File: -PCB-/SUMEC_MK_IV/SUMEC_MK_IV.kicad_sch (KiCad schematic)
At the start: 0 parts

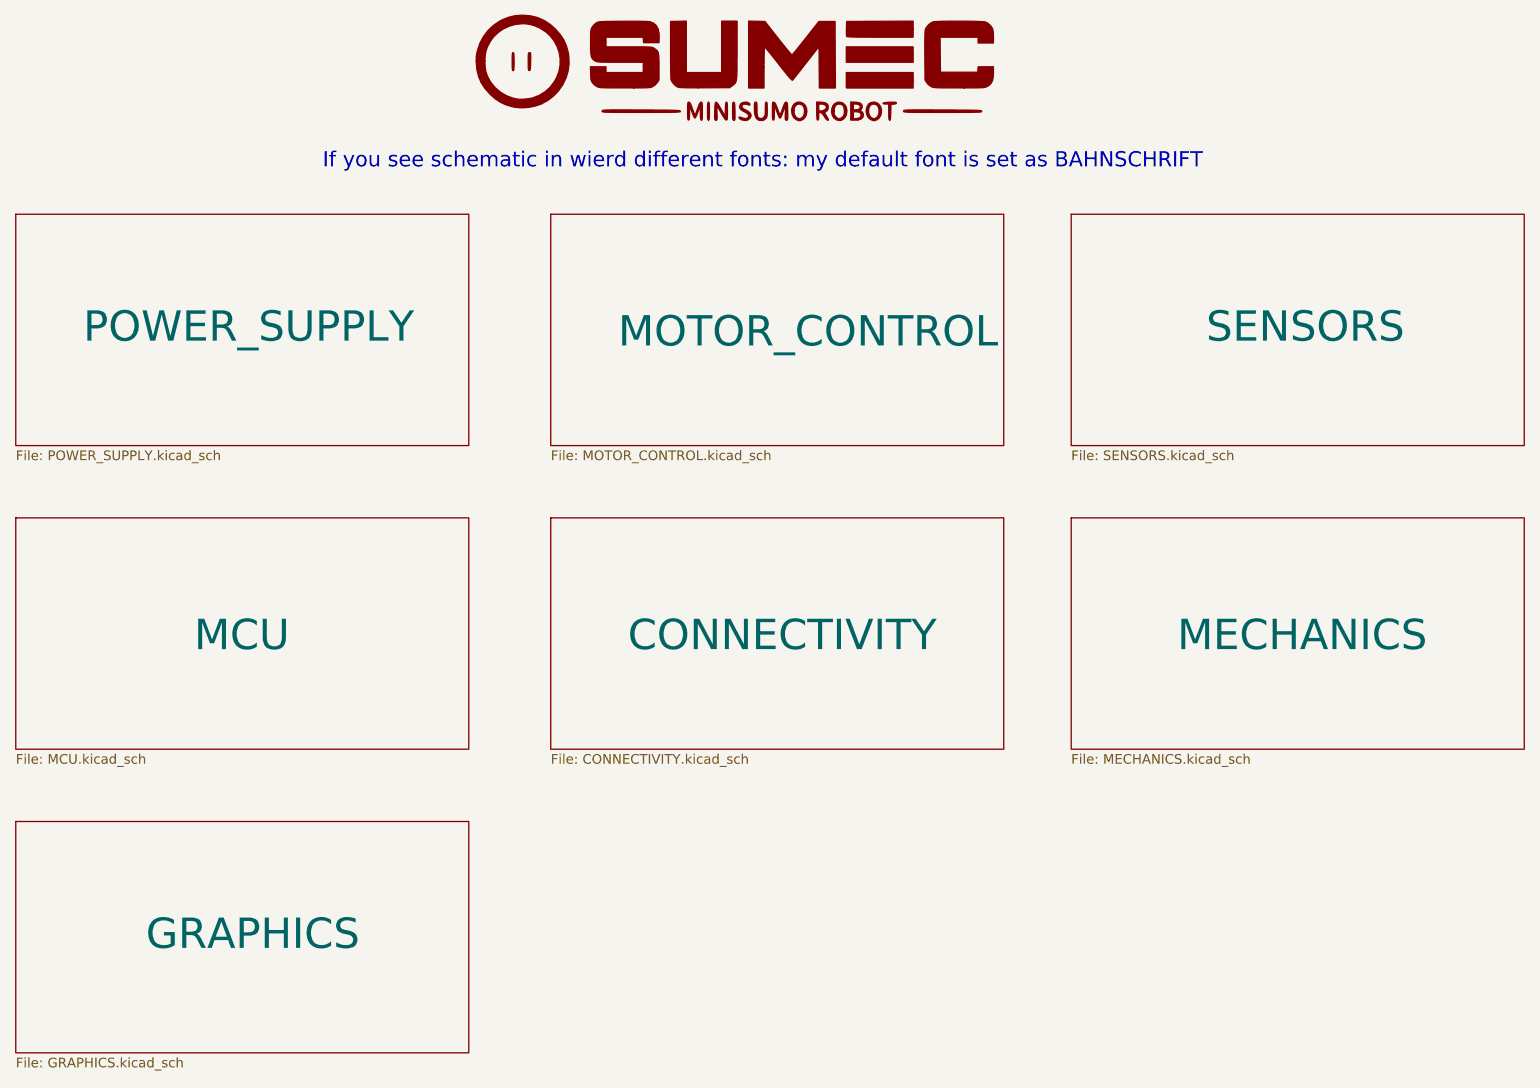
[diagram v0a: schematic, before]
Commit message: Minor text changes in schematic
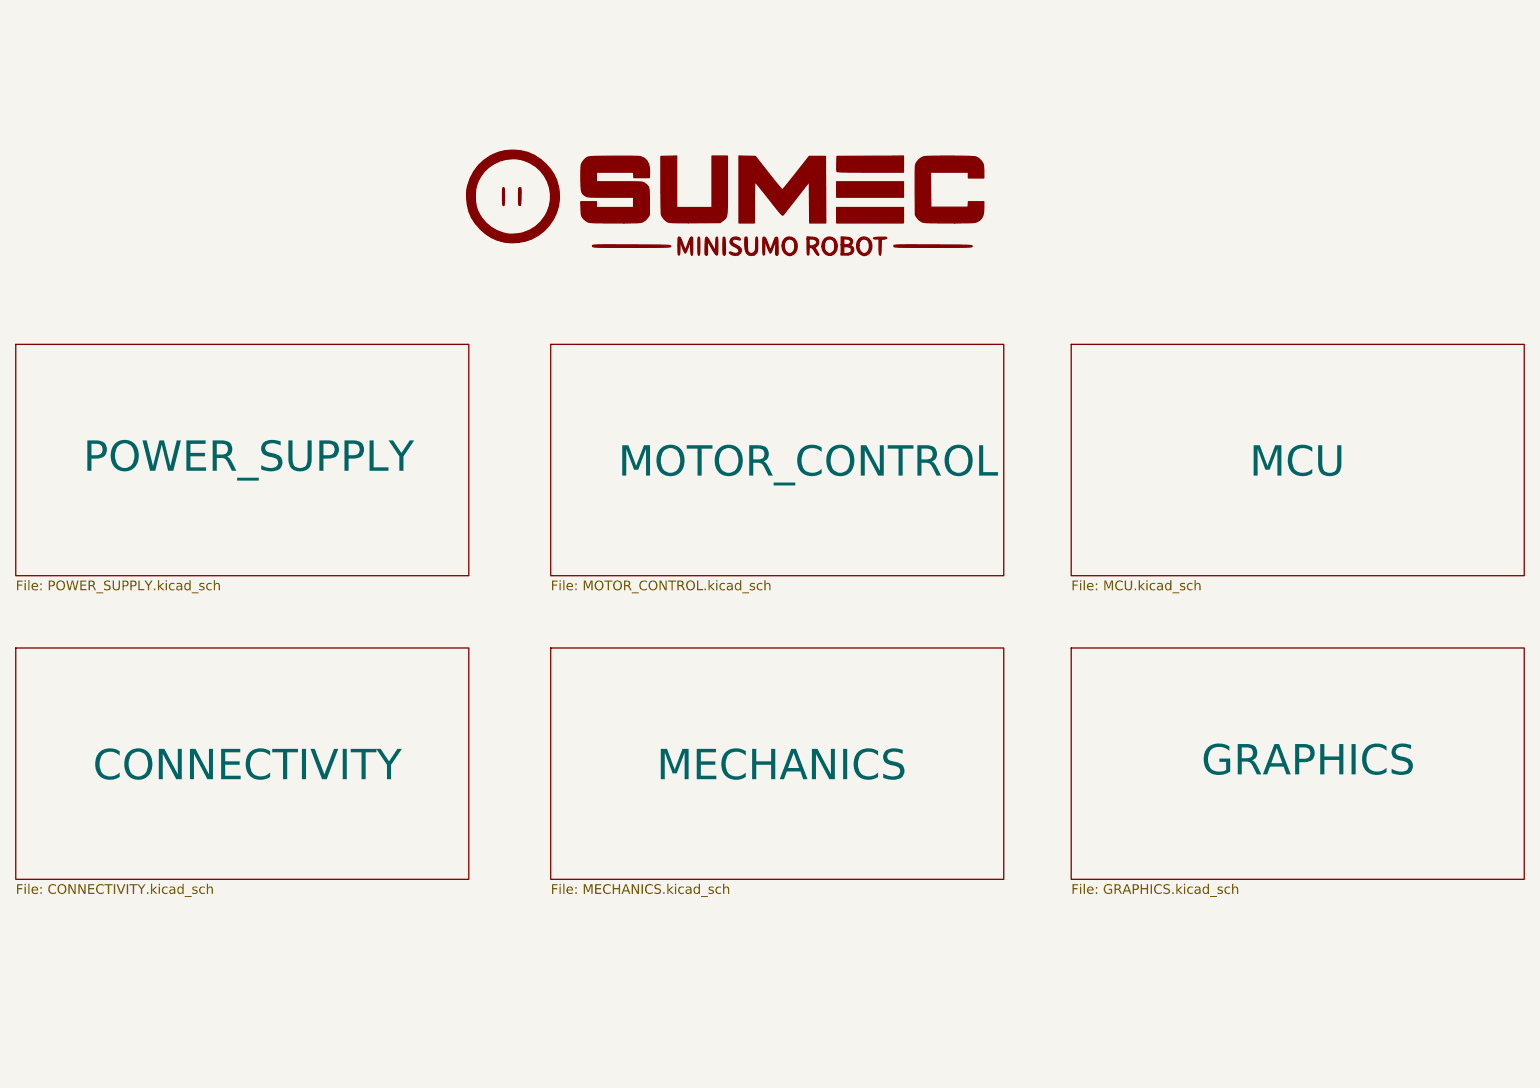
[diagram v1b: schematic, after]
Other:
- removed sheet SENSORS
- note removed: "If you see schematic in wierd different fonts: my default font is set as BAHNSCHRIFT"
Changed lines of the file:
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@@
 		(company "SPS NA PROSEKU")
 		(comment 1 "Made in Prague, Czech Republic")
-		(comment 2 "CONTACT: Savva Popov, menmenson09@gmail.com, +420 605 570 366")
-		(comment 3 "Made by Bismarx aka MenMenson")
+		(comment 2 "CONTACT: Savva Popov, savva.popov.sp@gmail.com, +420 605 570 366")
+		(comment 3 "Made by bismarx-v1")
 		(comment 4 "SUMEC MK IV aka SMD-V3 board")
-	)
-	(text "If you see schematic in wierd different fonts: my default font is set as BAHNSCHRIFT"
-		(exclude_from_sim no)
-		(at 147.32 41.91 0)
-		(effects
-			(font
-				(size 2 2)
-				(color 0 0 0 1)
-			)
-		)
 	)
 	(symbol
 		(lib_id "sumec_sch_lib:LOGO SMALL")
-		(at 142.24 30.48 0)
+		(at 140.97 48.26 0)
 		(unit 1)
 		(exclude_from_sim no)
@@
 		(fields_autoplaced yes)
 		(property "Reference" "#G1"
-			(at 142.24 19.8543 0)
+			(at 140.97 37.6343 0)
 			(effects
 				(font
@@
 		)
 		(property "Value" "LOGO SMALL"
-			(at 142.24 41.1057 0)
+			(at 140.97 58.8857 0)
 			(effects
 				(font
@@
 		)
 		(property "Footprint" ""
-			(at 142.24 30.48 0)
+			(at 140.97 48.26 0)
 			(effects
 				(font
@@
 		)
 		(property "Datasheet" ""
-			(at 142.24 30.48 0)
+			(at 140.97 48.26 0)
 			(effects
 				(font
@@
 		)
 		(property "Description" ""
-			(at 142.24 30.48 0)
+			(at 140.97 48.26 0)
 			(effects
 				(font
@@
 	)
 	(sheet
-		(at 48.895 88.9)
+		(at 187.96 66.04)
 		(size 59.69 30.48)
 		(stroke
@@
 		)
 		(property "Sheetname" "MCU"
-			(at 72.39 106.68 0)
+			(at 211.455 83.82 0)
 			(effects
 				(font
@@
 		)
 		(property "Sheetfile" "MCU.kicad_sch"
-			(at 48.895 119.9646 0)
+			(at 187.96 97.1046 0)
 			(effects
 				(font
@@
 		)
 		(property "Field2" ""
-			(at 48.895 88.9 0)
+			(at 187.96 66.04 0)
 			(effects
 				(font
@@
 	)
 	(sheet
-		(at 119.38 48.895)
+		(at 119.38 66.04)
 		(size 59.69 30.48)
 		(stroke
@@
 		)
 		(property "Sheetname" "MOTOR_CONTROL"
-			(at 128.27 66.675 0)
+			(at 128.27 83.82 0)
 			(effects
 				(font
@@
 		)
 		(property "Sheetfile" "MOTOR_CONTROL.kicad_sch"
-			(at 119.38 79.9596 0)
+			(at 119.38 97.1046 0)
 			(effects
 				(font
@@
 	)
 	(sheet
-		(at 187.96 48.895)
-		(size 59.69 30.48)
-		(stroke
-			(width 0.1524)
-			(type solid)
-			(color 0 0 0 1)
-		)
-		(fill
-			(color 255 255 255 1.0000)
-		)
-		(property "Sheetname" "SENSORS"
-			(at 205.74 66.04 0)
-			(effects
-				(font
-					(size 4 4)
-					(color 0 0 0 1)
-				)
-				(justify left bottom)
-			)
-		)
-		(property "Sheetfile" "SENSORS.kicad_sch"
-			(at 187.96 79.9596 0)
-			(effects
-				(font
-					(size 1.27 1.27)
-					(color 0 0 0 1)
-				)
-				(justify left top)
-			)
-		)
-		(instances
-			(project "SUMEC_MK_IV"
-				(path "/900bd7ac-cdf9-4a2f-8b1f-2c21e3760046"
-					(page "4")
-				)
-			)
-		)
-	)
-	(sheet
-		(at 187.96 88.9)
+		(at 119.38 106.045)
 		(size 59.69 30.48)
 		(stroke
@@
 		)
 		(property "Sheetname" "MECHANICS"
-			(at 201.93 106.68 0)
-			(effects
-				(font
+			(at 133.35 123.825 0)
+			(effects
+				(font
+					(face "Bahnschrift")
 					(size 4 4)
 					(color 0 0 0 1)
@@
 		)
 		(property "Sheetfile" "MECHANICS.kicad_sch"
-			(at 187.96 119.9646 0)
+			(at 119.38 137.1096 0)
 			(effects
 				(font
@@
 	)
 	(sheet
-		(at 119.38 88.9)
+		(at 48.895 106.045)
 		(size 59.69 30.48)
 		(stroke
@@
 		)
 		(property "Sheetname" "CONNECTIVITY"
-			(at 129.54 106.68 0)
+			(at 59.055 123.825 0)
 			(effects
 				(font
@@
 		)
 		(property "Sheetfile" "CONNECTIVITY.kicad_sch"
-			(at 119.38 119.9646 0)
+			(at 48.895 137.1096 0)
 			(effects
 				(font
@@
 		)
 		(property "Field2" ""
-			(at 119.38 88.9 0)
+			(at 48.895 106.045 0)
 			(effects
 				(font
@@
 	)
 	(sheet
-		(at 48.895 48.895)
+		(at 48.895 66.04)
 		(size 59.69 30.48)
 		(stroke
@@
 		)
 		(property "Sheetname" "POWER_SUPPLY"
-			(at 57.785 66.04 0)
-			(effects
-				(font
+			(at 57.785 83.185 0)
+			(effects
+				(font
+					(face "Bahnschrift")
 					(size 4 4)
 					(color 0 0 0 1)
@@
 		)
 		(property "Sheetfile" "POWER_SUPPLY.kicad_sch"
-			(at 48.895 79.9596 0)
+			(at 48.895 97.1046 0)
 			(effects
 				(font
@@
 	)
 	(sheet
-		(at 48.895 128.905)
+		(at 187.96 106.045)
 		(size 59.69 30.48)
 		(stroke
@@
 		)
 		(property "Sheetname" "GRAPHICS"
-			(at 66.04 146.05 0)
-			(effects
-				(font
+			(at 205.105 123.19 0)
+			(effects
+				(font
+					(face "Bahnschrift")
 					(size 4 4)
 					(color 0 0 0 1)
@@
 		)
 		(property "Sheetfile" "GRAPHICS.kicad_sch"
-			(at 48.895 159.9696 0)
-			(effects
-				(font
+			(at 187.96 137.1096 0)
+			(effects
+				(font
